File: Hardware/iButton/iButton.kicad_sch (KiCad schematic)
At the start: 29 parts, among them IC1 TSOP75338TR, J1 Conn_01x06, X1b1 PG-2.5-9.5-SM, X2b1 PG-2.5-8.0-SM, X3b1 PG-3.0-10.0-SM

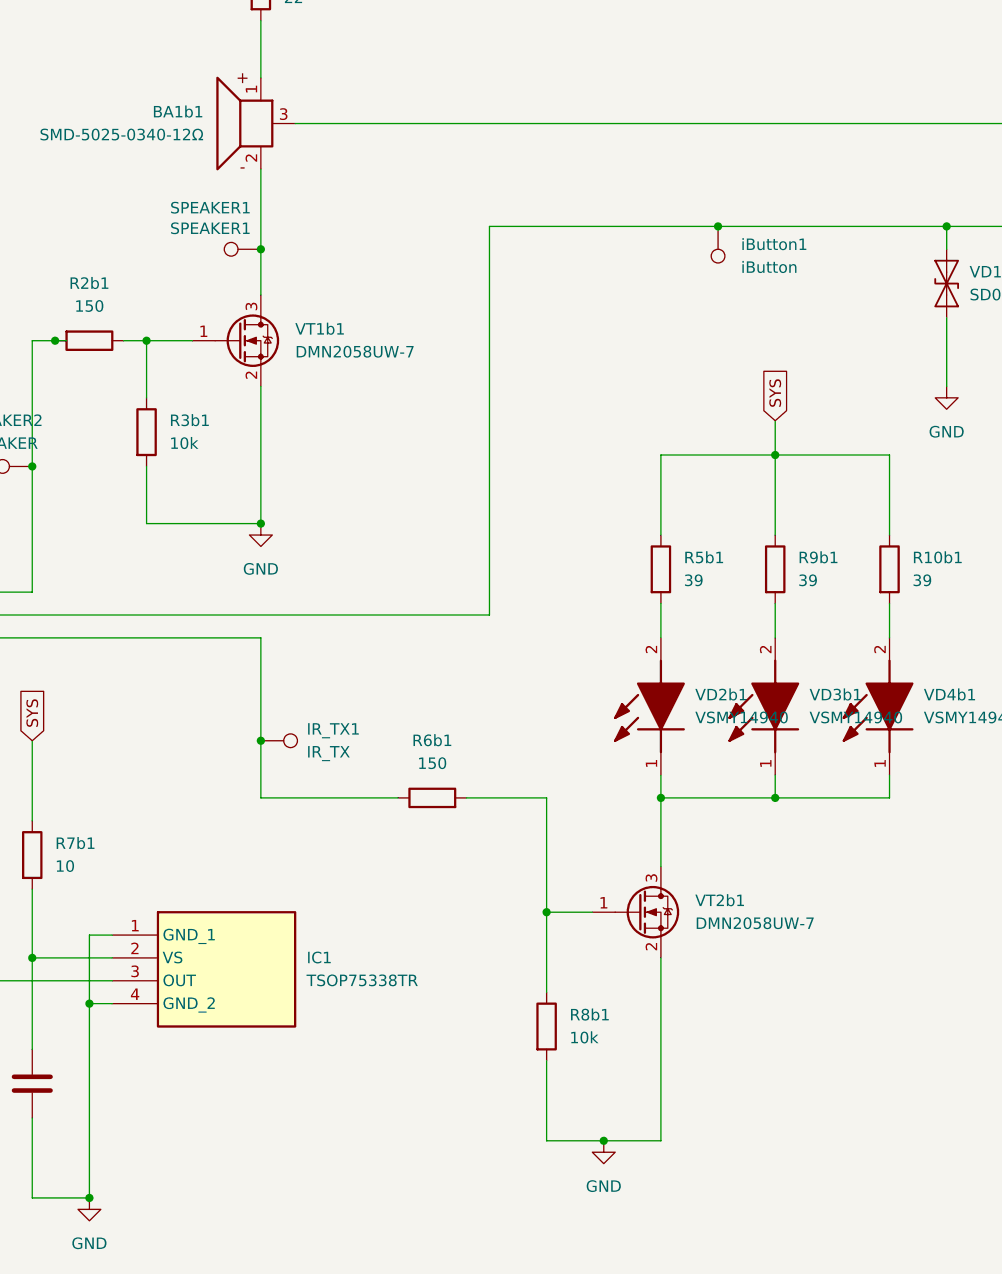
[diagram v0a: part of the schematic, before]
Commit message: PCB: fix bugs
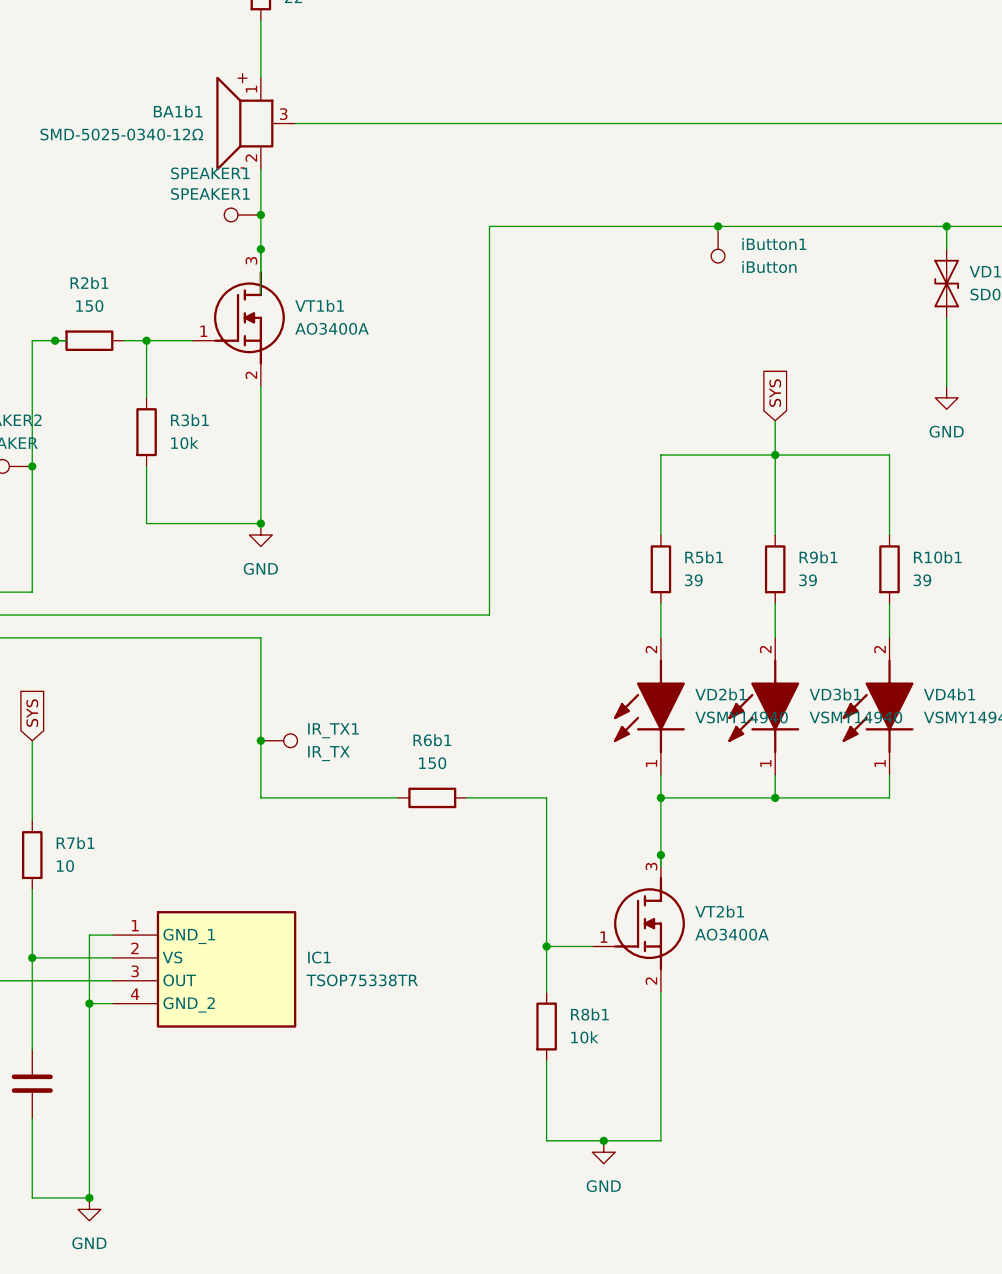
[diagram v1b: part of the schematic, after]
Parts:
- VT1b1, VT2b1: value DMN2058UW-7 -> AO3400A; footprint Package_TO_SOT_SMD:SOT-23 -> SOT95P280X125-3N; symbol Transistor_FET:DMN2058U -> SamacSys_Parts:AO3400A; Height (none) -> 1.25; Manufacturer_Name (none) -> Alpha & Omega Semiconductors; Manufacturer_Part_Number (none) -> AO3400A
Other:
- moved on the sheet: SPEAKER1
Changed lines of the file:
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@@
+	)
+	(junction
+		(at 158.75 143.51)
+		(diameter 0)
+		(color 0 0 0 0)
 	)
 	(junction
@@
 	)
 	(junction
-		(at 158.75 139.7)
+		(at 127 62.23)
 		(diameter 0)
 		(color 0 0 0 0)
@@
 	)
 	(junction
+		(at 171.45 133.35)
+		(diameter 0)
+		(color 0 0 0 0)
+	)
+	(junction
 		(at 82.55 120.65)
 		(diameter 0)
@@
 	(wire
 		(pts
+			(xy 127 62.23) (xy 127 66.04)
+		)
+		(stroke
+			(width 0)
+			(type default)
+		)
+	)
+	(wire
+		(pts
 			(xy 152.4 63.5) (xy 177.8 63.5)
 		)
@@
 	(wire
 		(pts
-			(xy 158.75 127) (xy 158.75 139.7)
-		)
-		(stroke
-			(width 0)
-			(type default)
-		)
-	)
-	(wire
-		(pts
 			(xy 19.05 106.68) (xy 152.4 106.68)
 		)
@@
 	(wire
 		(pts
-			(xy 127 57.15) (xy 127 66.04)
+			(xy 127 57.15) (xy 127 62.23)
 		)
 		(stroke
@@
 	(wire
 		(pts
-			(xy 158.75 139.7) (xy 163.83 139.7)
+			(xy 158.75 143.51) (xy 163.83 143.51)
 		)
 		(stroke
@@
 	(wire
 		(pts
-			(xy 171.45 144.78) (xy 171.45 165.1)
+			(xy 171.45 148.59) (xy 171.45 165.1)
+		)
+		(stroke
+			(width 0)
+			(type default)
+		)
+	)
+	(wire
+		(pts
+			(xy 127 81.28) (xy 127 96.52)
 		)
 		(stroke
@@
 	(wire
 		(pts
-			(xy 127 81.28) (xy 127 96.52)
+			(xy 158.75 143.51) (xy 158.75 148.59)
 		)
 		(stroke
@@
 	(wire
 		(pts
+			(xy 171.45 127) (xy 171.45 133.35)
+		)
+		(stroke
+			(width 0)
+			(type default)
+		)
+	)
+	(wire
+		(pts
 			(xy 184.15 85.09) (xy 184.15 88.9)
 		)
@@
 	(wire
 		(pts
+			(xy 171.45 133.35) (xy 171.45 134.62)
+		)
+		(stroke
+			(width 0)
+			(type default)
+		)
+	)
+	(wire
+		(pts
 			(xy 101.6 120.65) (xy 101.6 129.54)
 		)
@@
 	(wire
 		(pts
-			(xy 158.75 139.7) (xy 158.75 148.59)
-		)
-		(stroke
-			(width 0)
-			(type default)
-		)
-	)
-	(wire
-		(pts
-			(xy 171.45 127) (xy 171.45 134.62)
-		)
-		(stroke
-			(width 0)
-			(type default)
-		)
-	)
-	(wire
-		(pts
 			(xy 158.75 127) (xy 149.86 127)
 		)
@@
 		(pts
 			(xy 158.75 156.21) (xy 158.75 165.1)
+		)
+		(stroke
+			(width 0)
+			(type default)
+		)
+	)
+	(wire
+		(pts
+			(xy 158.75 127) (xy 158.75 143.51)
 		)
 		(stroke
@@
 	(symbol
 		(lib_id "Connector:TestPoint")
-		(at 127 66.04 90)
+		(at 127 62.23 90)
 		(unit 1)
 		(exclude_from_sim no)
@@
 		(dnp no)
 		(property "Reference" "SPEAKER1"
-			(at 121.412 61.468 90)
+			(at 121.412 57.658 90)
 			(effects
 				(font
@@
 		)
 		(property "Value" "SPEAKER1"
-			(at 121.412 63.754 90)
+			(at 121.412 59.944 90)
 			(effects
 				(font
@@
 		)
 		(property "Footprint" "TestPoint:TestPoint_Pad_1.0x1.0mm"
-			(at 127 60.96 0)
+			(at 127 57.15 0)
 			(effects
 				(font
@@
 		)
 		(property "Datasheet" "~"
-			(at 127 60.96 0)
+			(at 127 57.15 0)
 			(effects
 				(font
@@
 		)
 		(property "Description" "test point"
-			(at 127 66.04 0)
+			(at 127 62.23 0)
 			(effects
 				(font
@@
 	)
 	(symbol
-		(lib_id "Transistor_FET:DMN2058U")
-		(at 124.46 76.2 0)
+		(lib_id "SamacSys_Parts:AO3400A")
+		(at 119.38 76.2 0)
 		(unit 1)
 		(exclude_from_sim no)
@@
 		(fields_autoplaced yes)
 		(property "Reference" "VT1b1"
+			(at 130.81 72.3899 0)
+			(effects
+				(font
+					(size 1.27 1.27)
+				)
+				(justify left)
+			)
+		)
+		(property "Value" "AO3400A"
 			(at 130.81 74.9299 0)
 			(effects
@@
 			)
 		)
-		(property "Value" "DMN2058UW-7"
-			(at 130.81 77.4699 0)
-			(effects
-				(font
-					(size 1.27 1.27)
-				)
-				(justify left)
-			)
-		)
-		(property "Footprint" "Package_TO_SOT_SMD:SOT-23"
-			(at 129.54 78.105 0)
-			(effects
-				(font
-					(size 1.27 1.27)
-					(italic yes)
-				)
-				(justify left)
-				(hide yes)
-			)
-		)
-		(property "Datasheet" "http://www.diodes.com/assets/Datasheets/DMN2058U.pdf"
-			(at 129.54 80.01 0)
-			(effects
-				(font
-					(size 1.27 1.27)
-				)
-				(justify left)
-				(hide yes)
-			)
-		)
-		(property "Description" "4.6A Id, 20V Vds, N-Channel MOSFET, SOT-23"
-			(at 124.46 76.2 0)
-			(effects
-				(font
-					(size 1.27 1.27)
-				)
+		(property "Footprint" "SOT95P280X125-3N"
+			(at 130.81 174.93 0)
+			(effects
+				(font
+					(size 1.27 1.27)
+				)
+				(justify left top)
+				(hide yes)
+			)
+		)
+		(property "Datasheet" "http://aosmd.com/res/data_sheets/AO3400A.pdf"
+			(at 130.81 274.93 0)
+			(effects
+				(font
+					(size 1.27 1.27)
+				)
+				(justify left top)
+				(hide yes)
+			)
+		)
+		(property "Description" "30V N-Channel MOSFET"
+			(at 119.38 76.2 0)
+			(effects
+				(font
+					(size 1.27 1.27)
+				)
+				(hide yes)
+			)
+		)
+		(property "Height" "1.25"
+			(at 130.81 474.93 0)
+			(effects
+				(font
+					(size 1.27 1.27)
+				)
+				(justify left top)
+				(hide yes)
+			)
+		)
+		(property "Mouser Part Number" ""
+			(at 130.81 574.93 0)
+			(effects
+				(font
+					(size 1.27 1.27)
+				)
+				(justify left top)
+				(hide yes)
+			)
+		)
+		(property "Mouser Price/Stock" ""
+			(at 130.81 674.93 0)
+			(effects
+				(font
+					(size 1.27 1.27)
+				)
+				(justify left top)
+				(hide yes)
+			)
+		)
+		(property "Manufacturer_Name" "Alpha & Omega Semiconductors"
+			(at 130.81 774.93 0)
+			(effects
+				(font
+					(size 1.27 1.27)
+				)
+				(justify left top)
+				(hide yes)
+			)
+		)
+		(property "Manufacturer_Part_Number" "AO3400A"
+			(at 130.81 874.93 0)
+			(effects
+				(font
+					(size 1.27 1.27)
+				)
+				(justify left top)
 				(hide yes)
 			)
@@
 	)
 	(symbol
-		(lib_id "Transistor_FET:DMN2058U")
-		(at 168.91 139.7 0)
+		(lib_id "SamacSys_Parts:AO3400A")
+		(at 163.83 143.51 0)
 		(unit 1)
 		(exclude_from_sim no)
@@
 		(fields_autoplaced yes)
 		(property "Reference" "VT2b1"
-			(at 175.26 138.4299 0)
+			(at 175.26 139.6999 0)
 			(effects
 				(font
@@
 			)
 		)
-		(property "Value" "DMN2058UW-7"
-			(at 175.26 140.9699 0)
+		(property "Value" "AO3400A"
+			(at 175.26 142.2399 0)
 			(effects
 				(font
@@
 			)
 		)
-		(property "Footprint" "Package_TO_SOT_SMD:SOT-23"
-			(at 173.99 141.605 0)
-			(effects
-				(font
-					(size 1.27 1.27)
-					(italic yes)
-				)
-				(justify left)
-				(hide yes)
-			)
-		)
-		(property "Datasheet" "http://www.diodes.com/assets/Datasheets/DMN2058U.pdf"
-			(at 173.99 143.51 0)
-			(effects
-				(font
-					(size 1.27 1.27)
-				)
-				(justify left)
-				(hide yes)
-			)
-		)
-		(property "Description" "4.6A Id, 20V Vds, N-Channel MOSFET, SOT-23"
-			(at 168.91 139.7 0)
-			(effects
-				(font
-					(size 1.27 1.27)
-				)
-				(hide yes)
-			)
+		(property "Footprint" "SOT95P280X125-3N"
+			(at 175.26 242.24 0)
+			(effects
+				(font
+					(size 1.27 1.27)
+				)
+				(justify left top)
+				(hide yes)
+			)
+		)
+		(property "Datasheet" "http://aosmd.com/res/data_sheets/AO3400A.pdf"
+			(at 175.26 342.24 0)
+			(effects
+				(font
+					(size 1.27 1.27)
+				)
+				(justify left top)
+				(hide yes)
+			)
+		)
+		(property "Description" "30V N-Channel MOSFET"
+			(at 163.83 143.51 0)
+			(effects
+				(font
+					(size 1.27 1.27)
+				)
+				(hide yes)
+			)
+		)
+		(property "Height" "1.25"
+			(at 175.26 542.24 0)
+			(effects
+				(font
+					(size 1.27 1.27)
+				)
+				(justify left top)
+				(hide yes)
+			)
+		)
+		(property "Mouser Part Number" ""
+			(at 175.26 642.24 0)
+			(effects
+				(font
+					(size 1.27 1.27)
+				)
+				(justify left top)
+				(hide yes)
+			)
+		)
+		(property "Mouser Price/Stock" ""
+			(at 175.26 742.24 0)
+			(effects
+				(font
+					(size 1.27 1.27)
+				)
+				(justify left top)
+				(hide yes)
+			)
+		)
+		(property "Manufacturer_Name" "Alpha & Omega Semiconductors"
+			(at 175.26 842.24 0)
+			(effects
+				(font
+					(size 1.27 1.27)
+				)
+				(justify left top)
+				(hide yes)
+			)
+		)
+		(property "Manufacturer_Part_Number" "AO3400A"
+			(at 175.26 942.24 0)
+			(effects
+				(font
+					(size 1.27 1.27)
+				)
+				(justify left top)
+				(hide yes)
+			)

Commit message: PCB: add "remove from bom" entity; adjust design rule
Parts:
- GND1, IR_RX1, IR_TX1, SPEAKER1, SPEAKER2, SYS1, iButton1: now left out of the parts list
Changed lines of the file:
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@@
 		(unit 1)
 		(exclude_from_sim no)
-		(in_bom yes)
+		(in_bom no)
 		(on_board yes)
 		(dnp no)
@@
 		(unit 1)
 		(exclude_from_sim no)
-		(in_bom yes)
+		(in_bom no)
 		(on_board yes)
 		(dnp no)
@@
 		(unit 1)
 		(exclude_from_sim no)
-		(in_bom yes)
+		(in_bom no)
 		(on_board yes)
 		(dnp no)
@@
 		(unit 1)
 		(exclude_from_sim no)
-		(in_bom yes)
+		(in_bom no)
 		(on_board yes)
 		(dnp no)
@@
 		(unit 1)
 		(exclude_from_sim no)
-		(in_bom yes)
+		(in_bom no)
 		(on_board yes)
 		(dnp no)
@@
 		(unit 1)
 		(exclude_from_sim no)
-		(in_bom yes)
+		(in_bom no)
 		(on_board yes)
 		(dnp no)
@@
 		(unit 1)
 		(exclude_from_sim no)
-		(in_bom yes)
-		(on_board yes)
-		(dnp no)
+		(in_bom no)
+		(on_board yes)
+		(dnp no)
